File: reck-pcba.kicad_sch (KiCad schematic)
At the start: 0 parts

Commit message: Added ESP32, Power, LEDs, IMU, and GPS - Added supporting libraries - Added datasheets in the doc/datasheet folder
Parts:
- added C1, C13, C14, C17, C18, C19, C2, C20, C23, C24, C28, C29, C3, C30, C31, C4: 100nF, symbol Device:C
- added C10, C11, C15, C21, C22, C25, C6, C7: 1uF, symbol Device:C
- added C12, C9: 100n, symbol Device:C
- added C16, C5, C8: 10uF, symbol Device:C
- added C26, C27: 3.3pF, symbol Device:C
- added D1, D2, D3: LED, symbol Device:LED
- added J2: USB_C_Receptacle_USB2.0_16P, symbol reck-connectors:USB_C_Receptacle_USB2.0_16P
- added L1, L2, L3: 2.2n, symbol Device:L
- added R1, R13, R14, R15, R2, R3, R8: 5.1k, symbol Device:R
- added R10, R9: 150R, symbol Device:R
- added R11: 300R, symbol Device:R
- added R12, R6, R7: 49.9R, symbol Device:R
- added R4: 47R, symbol Device:R
- added R5: 470R, symbol Device:R
- added SW1: SW_Push, symbol Switch:SW_Push
- added TP1, TP2, TP3, TP4, TP5, TP6: TestPoint, TestPoint:TestPoint_Pad_D1.5mm, symbol Connector:TestPoint
- added U1: ESP32-C3FH4, reck-ics:QFN-32-1EP_5x5mm_P0.5mm_EP3.7x3.7mm, symbol reck-ics:ESP32-C3FH4
- added U10: USBLC6-2P6, Package_TO_SOT_SMD:SOT-666, symbol Power_Protection:USBLC6-2P6
- added U11, U7, U8, U9: WS2812B, reck-ics:WS2812B, symbol reck-ics:WS2812B
- added U12: SAM-M10Q-00B, reck-ics:SAM-M10Q, symbol reck-ics:SAM-M10Q-00B
- added U2: SN74LVC1T45DBV, Package_TO_SOT_SMD:SOT-23-6, symbol Logic_LevelTranslator:SN74LVC1T45DBV
- added U3, U4: NCP705MT33TCG, reck-ics:DFN-6-1EP_2x2mm_P0.65mm_EP1.01x1.7mm, symbol reck-ics:NCP705MT33TCG
- added U5: ISM330DHCXTR, reck-ics:LGA-14L_2.5x3.0mm_P0.5mm, symbol reck-ics:ISM330DHCXTR
- added Y2: 40MHz, symbol Device:Crystal_GND2
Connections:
- new net: U11.4 (DI), U2.4 (B)
- new net: D1.1 (K), R9.1
- new net: J2.A5 (CC1), R2.1
- new net: U11.3 (GND), U7.3 (GND), U8.3 (GND), U9.3 (GND)
- new net: U8.2 (DO), U9.4 (DI)
- new net: C26.1, L3.1, U1.1 (LNA_IN)
- new net: C27.1, L3.2
- new net: J2.A7 (D-), J2.B7 (D-), U10.1 (I/O1)
- new net: J2.A6 (D+), J2.B6 (D+), U10.3 (I/O2)
- new net: R7.2, U1.12 (MTCK)
- new net: R6.2, U1.13 (MTDO)
- new net: C13.1, L2.1, U1.2 (VDD3P3), U1.3 (VDD3P3)
- new net: R5.2, U1.28 (U0TXD)
- new net: C24.1, U1.29 (XTAL_N), Y2.3
- new net: R4.1, U1.30 (XTAL_P)
- new net: C25.1, R3.2, SW1.1, U1.7 (CHIP_EN)
- new net: C23.1, R4.2, Y2.1
- new net: D3.1 (K), R11.1
- new net: J2.B5 (CC2), R1.1
- new net: U11.2 (DO), U7.4 (DI)
- new net: D2.1 (K), R10.1
- new net: R12.2, U5.1 (SDO/SA0)
- new net: U7.2 (DO), U8.4 (DI)
- new net +3V3A: C10.1, C11.1, C28.1, C29.1, C8.1, D1.2 (A), D2.2 (A), R8.1, U12.17 (VCC), U12.2 (V_IO), U12.3 (V_BCKP), U3.1 (OUT), U5.5 (VDD_IO), U5.8 (VDD)
- new net +3V3D: C14.1, C15.1, C16.1, C17.1, C18.1, C19.1, C20.1, C21.1, C22.1, C31.1, C5.1, L2.2, R13.1, R14.1, R15.1, R3.1, U1.11 (VDD3P3_RTC), U1.17 (VDD3P3_CPU), U1.18 (VDD_SPI), U1.31 (VDDA), U1.32 (VDDA), U2.1 (VCCA), U2.5 (DIR), U4.1 (OUT)
- new net +5V: C1.1, C2.1, C3.1, C30.1, C4.1, U11.1 (VDD), U2.6 (VCCB), U7.1 (VDD), U8.1 (VDD), U9.1 (VDD)
- new net +VBUS: C9.1, D3.2 (A), J2.A4 (VBUS), J2.A9 (VBUS), J2.B4 (VBUS), J2.B9 (VBUS), L1.1, U10.5 (VBUS)
- new net +VBUS-FILT: C12.1, C6.1, C7.1, L1.2, U3.4 (EN), U3.6 (IN), U4.4 (EN), U4.6 (IN)
- new net GND: C1.2, C10.2, C11.2, C12.2, C13.2, C14.2, C15.2, C16.2, C17.2, C18.2, C19.2, C2.2, C20.2, C21.2, C22.2, C23.2, C24.2, C25.2, C26.2, C27.2, C28.2, C29.2, C3.2, C30.2, C31.2, C4.2, C5.2, C6.2, C7.2, C8.2, C9.2, J2.A1 (GND), J2.A12 (GND), J2.B1 (GND), J2.B12 (GND), R1.2, R10.2, R11.2, R2.2, R9.2, SW1.2, U1.33 (GND), U10.2 (GND), U12.1 (GND), U12.10 (GND), U12.11 (GND), U12.15 (GND), U12.16 (GND), U12.20 (GND), U12.4 (GND), U12.5 (GND), U12.6 (GND), U2.2 (GND), U3.2 (NC), U3.3 (GND), U3.5 (NC), U3.7 (EP), U4.2 (NC), U4.3 (GND), U4.5 (NC), U4.7 (EP), U5.2 (SDX), U5.3 (SCX), U5.6 (GND), U5.7 (GND), Y2.2
- new net GPIO10: U1.16 (GPIO10)
- new net GPIO8: U1.14 (GPIO8)
- new net GPIO9: U1.15 (GPIO9)
- new net GPS-EXTINT: U12.19 (EXTINT)
- new net GPS-NRESET: R8.2, U12.18 (~{RESET})
- new net GPS-TP: TP5.1, U12.7 (TIMEPULSE)
- new net IMU-CS: U5.12 (CS)
- new net IMU-INT1: U5.4 (INT1)
- new net IMU-INT2: U5.9 (INT2)
- new net LED-DOUT: U1.8 (GPIO3), U2.3 (A)
- new net MISO: R12.1, R13.2, TP6.1, U1.6 (GPIO2)
- new net MOSI: R6.1, TP4.1, U5.14 (SDA)
- new net SCL: R15.2, U1.9 (MTMS)
- new net SCLK: R7.1, TP3.1, U5.13 (SCL)
- new net SDA: R14.2, U1.10 (MTDI)
- new net UART0-RX: TP1.1, U1.27 (U0RXD), U12.13 (TXD)
- new net UART0-TX: R5.1, TP2.1, U12.14 (RXD)
- new net USB-DN: U1.25 (GPIO18), U10.6 (I/O1)
- new net USB-DP: U1.26 (GPIO19), U10.4 (I/O2)
- no-connect marks 0 -> 15
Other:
- note added: "GPIO2 MUST BE FLOATING GPIO8 MUST BE FLOATING GPIO9 MUST BE PULL-UP (PULL-UP INTERNAL) GPIO10 SPI2 CS0"
- note added: "Near VDD3P3_CPU"
- note added: "Near VDD3P3_RTC"
- note added: "Near VDD_A"
- note added: "Near VDD_SPI"
- note added: "Z=35R+10j"
- note added: "Z=50R"

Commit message: Added new uC, Power, and Motor support - Updated ESP32-C3 to ESP32-S3 due to GPIO constraints - Using two buck regulators for servo 5V power and board 3V3
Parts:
- removed C5: 10uF, symbol Device:C
- removed R6: 49.9R, symbol Device:R
- removed SW1: SW_Push, symbol Switch:SW_Push
- removed TP1, TP2, TP3, TP4, TP5, TP6: TestPoint, TestPoint:TestPoint_Pad_D1.5mm, symbol Connector:TestPoint
- removed U1: ESP32-C3FH4, reck-ics:QFN-32-1EP_5x5mm_P0.5mm_EP3.7x3.7mm, symbol reck-ics:ESP32-C3FH4
- removed U10: USBLC6-2P6, Package_TO_SOT_SMD:SOT-666, symbol Power_Protection:USBLC6-2P6
- removed U3, U4: NCP705MT33TCG, reck-ics:DFN-6-1EP_2x2mm_P0.65mm_EP1.01x1.7mm, symbol reck-ics:NCP705MT33TCG
- removed Y2: 40MHz, symbol Device:Crystal_GND2
- added C32, C33: 100nF, symbol Device:C
- added C34: 4.7nF, symbol Device:C
- added C36: 1uF, symbol Device:C
- added C41: 10uF, symbol Device:C
- added C5: 47uF, symbol Device:C_Polarized
- added D4: LED, symbol Device:LED
- added J4: Conn_01x03_Pin, Connector_PinHeader_2.54mm:PinHeader_1x03_P2.54mm_Vertical, symbol Connector:Conn_01x03_Pin
- added R16: 49.9R, symbol Device:R
- added R17, R24, R31, R32, R33: 5.1k, symbol Device:R
- added R23: R_Photo, symbol Device:R_Photo
- added SW1, SW2, SW3, SW4: PTS810_SJM_250_SMTR_LFS, reck-switches:PTS810_SJM_250_SMTR_LFS, symbol reck-switches:PTS810_SJM_250_SMTR_LFS
- added TH1: Thermistor_NTC, symbol Device:Thermistor_NTC
- added U1: ECS-2520S33-400-FN-TR, Oscillator:Oscillator_SMD_EuroQuartz_XO32-4Pin_3.2x2.5mm, symbol Oscillator:KC2520Z
- added U10: SN74LVC1T45DBV, Package_TO_SOT_SMD:SOT-23-6, symbol Logic_LevelTranslator:SN74LVC1T45DBV
- added U13: MCP4728, Package_SO:MSOP-10_3x3mm_P0.5mm, symbol Analog_DAC:MCP4728
- added U3: DRV8231ADSGR, Package_SON:WSON-8-1EP_2x2mm_P0.5mm_EP0.9x1.6mm, symbol reck-ics:DRV8231ADSGR
- added U4: USBLC6-2P6, Package_TO_SOT_SMD:SOT-666, symbol Power_Protection:USBLC6-2P6
- added U6: ESP32-S3FN8, reck-ics:QFN-56-1EP_7x7mm_P0.4mm_EP4x4mm, symbol reck-ics:ESP32-S3FN8
- C12, C9: value 100n -> 100nF
- C23: value 100nF -> 20pF
- C6: value 1uF -> 100nF
- C7: value 1uF -> 100n
- C8: value 10uF -> 100n
- J2: footprint (none) -> Connector_USB:USB_C_Receptacle_GCT_USB4105-xx-A_16P_TopMnt_Horizontal
- R1: value 5.1k -> 1M
- R10, R9: value 150R -> 330R
- R11: value 300R -> 660R
- R14: value 5.1k -> 499R
- R15: value 5.1k -> 330R
- R4: value 47R -> 5.1k
- R5: value 470R -> 5.1k
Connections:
- net +5V is gone; now on net +VBUS-FILT: C1.1, C2.1, C3.1, C30.1, C4.1, U11.1 (VDD), U2.6 (VCCB), U7.1 (VDD), U8.1 (VDD), U9.1 (VDD)
- net +VBUS: now also C7.1, U4.5 (VBUS); no longer C9.1, D3.2 (A)
- net +VBUS-FILT: now also C8.1, D3.2 (A); no longer C12.1, C6.1, C7.1
- net GND: now also R15.2, U11.3 (GND), U7.3 (GND), U8.3 (GND), U9.3 (GND), C32.2, C33.2, C36.2, C41.2, C5.2, J4.3 (Pin_3), R17.2, R24.2, R33.2, SW1.1, SW1.2, SW2.1, SW2.2, SW3.1, SW3.2, SW4.1, SW4.2, U1.2 (GND), U10.2 (GND), U13.10 (VSS), U13.4 (~{LDAC}), U3.7 (GND), U3.9 (EP), U6.57 (GND); no longer C23.2, R1.2
- net IMU-CS: now also R32.2
- net MISO: now also R4.2, U6.18 (GPIO13/MISO); no longer R13.2
- net MOSI: now also R16.1
- net SCL: now also U13.2 (SCL); no longer R15.2
- net SDA: now also U13.3 (SDA); no longer R14.2
- net UART0-RX: now also U6.50 (U0RXD/GPIO44)
- net UART0-TX: now also R14.2; no longer R5.1
- net USB-DN: now also U4.6 (I/O1), U6.25 (USB_D-/GPIO19)
- net USB-DP: now also U4.4 (I/O2), U6.26 (USB_D+/GPIO20)
- net at J2.A5 (CC1): now also R17.1; no longer R2.1
- net at C26.1, L3.1: now also U6.1 (LNA_IN)
- net at J2.A7 (D-), J2.B7 (D-): now also U4.1 (I/O1)
- net at J2.A6 (D+), J2.B6 (D+): now also U4.3 (I/O2)
- net at R7.2: now also U6.17 (GPIO12/SCLK)
- net at C13.1, L2.1: now also U6.2 (VDD3P3), U6.3 (VDD3P3)
- net BOOT-SEL: now reaches R5.2
- net BOOT-SEL: now also SW1.3, SW1.4
- net +3V3: now reaches C24.1
- net +3V3: now also C10.1, C11.1, C14.1, C15.1, C16.1, C17.1, C18.1, C19.1, C20.1, C22.1, C28.1, C29.1, C31.1, C9.1, D2.2 (A), L2.2, R13.1, R3.1, R4.1, R5.1, R8.1, U12.17 (VCC), U12.2 (V_IO), U12.3 (V_BCKP), U2.1 (VCCA), U2.5 (DIR), U5.5 (VDD_IO), U5.8 (VDD), C33.1, C36.1, C41.1, R23.1, R31.1, R32.1, U1.4 (VCC), U10.1 (VCCA), U10.5 (DIR), U13.1 (VDD), U3.4 (VREF), U6.20 (VDD3P3_RTC), U6.46 (VDD3P3_CPU), U6.55 (VDDA), U6.56 (VDDA)
- net ESP-NRESET: now reaches C25.1, R3.2
- net ESP-NRESET: now also SW2.3, SW2.4, U6.4 (CHIP_PU)
- net at C23.1: now also U6.54 (XTAL_P); no longer R4.2
- net at J2.B5 (CC2): now also R2.1; no longer R1.1
- net at J2.S1 (SHIELD): now also R1.1, C34.1
- removed net +3V3A: C10.1, C11.1, C28.1, C29.1, C8.1, D1.2 (A), D2.2 (A), R8.1, U12.17 (VCC), U12.2 (V_IO), U12.3 (V_BCKP), U5.5 (VDD_IO), U5.8 (VDD)
- removed net +3V3D: C14.1, C15.1, C16.1, C17.1, C18.1, C19.1, C20.1, C21.1, C22.1, C31.1, L2.2, R13.1, R14.1, R15.1, R3.1, U2.1 (VCCA), U2.5 (DIR)
- net GPS-TP renamed GPS-TIMEPULSE
- net LED-DOUT renamed DOUT-LED
- new net: D4.1 (K), R15.1
- new net: R16.2, U6.16 (GPIO11/MOSI)
- new net: C23.2, U1.3 (CLK)
- new net: R33.1, U3.1 (IPROPI)
- new net: J4.2 (Pin_2), U10.4 (B)
- new net: R14.1, U6.49 (U0TXD/GPIO43)
- new net +12V-EXT: C5.1, C6.1, U3.5 (VM)
- new net +5V-EXT: C12.1, J4.1 (Pin_1), U10.6 (VCCB)
- new net +VDD_SPI: C21.1, C32.1, U6.29 (VDD_SPI)
- new net AOUT-A: U13.6 (VOUTA)
- new net AOUT-B: U13.7 (VOUTB)
- new net AOUT-C: U13.8 (VOUTC)
- new net AOUT-D: U13.9 (VOUTD)
- new net BUTTON0: R31.2, SW4.3, SW4.4
- new net BUTTON1: R13.2, SW3.3, SW3.4
- new net LED0: D4.2 (A)
- new net LED1: D1.2 (A)
- new net MOTOR-IN1: U3.3 (IN1)
- new net MOTOR-IN2: U3.2 (IN2)
- new net MOTOR-OUT1: U3.6 (OUT1)
- new net MOTOR-OUT2: U3.8 (OUT2)
- new net PWM-SERVO: U10.3 (A)
- new net SHIELD: C34.2, R1.2, U4.2 (GND)
- new net V-PHOTO-RES: R23.2, R24.1
- no-connect marks 15 -> 13
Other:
- added sheet power (power.kicad_sch)
- note added: "0.43A Motor Current"
- note added: "BOOT SEL"
- note added: "BUTTON INPUTS"
- note added: "DIGITAL TO ANALOG CONVERTER (DAC)"
- note added: "GPS MODULE"
- note added: "HW RESET"
- note added: "I2C Address: 0x60"
- note added: "INDICATION LEDS"
- note added: "INERTIAL MEASUREMENT UNIT"
- note added: "LED STRIP"
- note added: "RECK (Resourceful Embedded Circuity Kit) PCBA"
- note added: "SERVO"
- note added: "USBC POWER AND DATA INPUT"
- note added: "USER BUTTON0"
- note added: "USER BUTTON1"
- note removed: "GPIO2 MUST BE FLOATING GPIO8 MUST BE FLOATING GPIO9 MUST BE PULL-UP (PULL-UP INTERNAL) GPIO10 SPI2 CS0"
- note removed: "Near VDD_SPI"
- moved on the sheet: C1, C10, C11, C13, C14, C15, C16, C17, C18, C19, C2, C20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

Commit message: Full Schematics Complete - Changed uC to ESP32-S3-WROOM-2 to allow for pinout discussion. - Moved buck regulators to main sheet. - Added titles and descriptions to each Sensor, Interface, or concept. - Added LCD. - Changed DAC to single-channel variant. - Added I2C Laser Time-of-Flight Sensor. - Added Environmental Sensor. - Updated pinout on uC.
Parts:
- removed C21: 1uF, symbol Device:C
- removed C23: 20pF, symbol Device:C
- removed C26: 3.3pF, symbol Device:C
- removed C31, C33: 100nF, symbol Device:C
- removed C41: 10uF, symbol Device:C
- removed L3: 2.2n, symbol Device:L
- removed R12, R16, R7: 49.9R, symbol Device:R
- removed R33, R4, R8: 5.1k, symbol Device:R
- removed SW3: PTS810_SJM_250_SMTR_LFS, reck-switches:PTS810_SJM_250_SMTR_LFS, symbol reck-switches:PTS810_SJM_250_SMTR_LFS
- removed TH1: Thermistor_NTC, symbol Device:Thermistor_NTC
- removed U1: ECS-2520S33-400-FN-TR, Oscillator:Oscillator_SMD_EuroQuartz_XO32-4Pin_3.2x2.5mm, symbol Oscillator:KC2520Z
- removed U10, U2: SN74LVC1T45DBV, Package_TO_SOT_SMD:SOT-23-6, symbol Logic_LevelTranslator:SN74LVC1T45DBV
- removed U12: SAM-M10Q-00B, reck-ics:SAM-M10Q, symbol reck-ics:SAM-M10Q-00B
- removed U13: MCP4728, Package_SO:MSOP-10_3x3mm_P0.5mm, symbol Analog_DAC:MCP4728
- removed U6: ESP32-S3FN8, reck-ics:QFN-56-1EP_7x7mm_P0.4mm_EP4x4mm, symbol reck-ics:ESP32-S3FN8
- added BZ1: CEM-1206S, reck-audio:CEM-1206S, symbol reck-audio:CEM-1206S
- added C2, C3, C37, C4, C5: 10uF, symbol Device:C
- added C34, C35: 100nF, symbol Device:C
- added D2: LED, symbol Device:LED
- added D3, D8: D_Schottky, symbol Device:D_Schottky
- added D5: D_Zener, symbol Device:D_Zener
- added J2, J3: 575-4, reck-connectors:575-4, symbol reck-connectors:575-4
- added J5: Conn_01x03_Pin, Connector_PinHeader_2.54mm:PinHeader_1x03_P2.54mm_Vertical, symbol Connector:Conn_01x03_Pin
- added J6: TBL002A-350-02GR-2OR, reck-connectors:TBL002A-350-02GR-2OR, symbol reck-connectors:TBL002A-350-02GR-2OR
- added Q1: BC846, Package_TO_SOT_SMD:SOT-23, symbol Transistor_BJT:BC846
- added R17, R18, R19, R22, R24, R25, R26, R28, R30, R31: 5.1k, symbol Device:R
- added R20: 330R, symbol Device:R
- added R21: 16k, symbol Device:R
- added R23: 26.7k, symbol Device:R
- added R27, R6: 1k, symbol Device:R
- added R3: 3.3k, symbol Device:R
- added RV1, RV2: 10k, symbol Device:R_Potentiometer
- added TP1, TP10, TP11, TP12, TP13, TP2, TP3, TP4, TP5, TP6, TP7, TP8, TP9: TestPoint, symbol Connector:TestPoint
- added U13: VL53L0CXV0DH1, Sensor_Distance:ST_VL53L1x, symbol Sensor_Distance:VL53L0CXV0DH1
- added U14: MCP4725A0T-E/CH, Package_TO_SOT_SMD:SOT-23-6, symbol Analog_DAC:MCP4725xxx-xCH
- added U16: BME280, Package_LGA:Bosch_LGA-8_2.5x2.5mm_P0.65mm_ClockwisePinNumbering, symbol Sensor:BME280
- added U2: LCD2X16, reck-ics:LCD2X16, symbol reck-ics:LCD2X16
- added U3, U4: TPS62912RPUR, reck-ics:VQFN-HR-10_2x2mm, symbol reck-ics:TPS62912RPUR
- added U5, U9: TXU0104PWR, Package_SO:TSSOP-14_4.4x5mm_P0.65mm, symbol reck-ics:TXU0104PWR
- added U8: ESP32-S3-WROOM-2, RF_Module:ESP32-S3-WROOM-2, symbol RF_Module:ESP32-S3-WROOM-2
- C11, C15, C22, C36: value 1uF -> 100nF
- C13, C14, C17, C18, C19, C24: value 100nF -> 22uF
- C16: value 10uF -> 22uF
- C27: value 3.3pF -> 100nF
- C7, C8: value 100n -> 2.2nF
- C9: value 100nF -> 1uF
- J1: renamed from J2; value USB_C_Receptacle_USB2.0_16P -> USB4105-GF-A
- L1, L2: value 2.2n -> 2.2uH
- R13: value 5.1k -> 6.04k
- R14: value 499R -> 6.04k
- R15: renamed from R23; value R_Photo -> 02-LDR4
- R8: renamed from R11; value 660R -> 1k
- renumbered C34 to C1, C1 to C21, C2 to C23, C3 to C25, C5 to C26, C6 to C28, C4 to C29, C29 to C31, C28 to C33, C25 to C6, D3 to D4, D2 to D6, D4 to D7, R3 to R11, R15 to R12, R24 to R16, R31 to R2, R32 to R29, R2 to R4, R17 to R5, R5 to R7, SW4 to SW1, SW1 to SW2, SW2 to SW3, U4 to U1, U8 to U10, U3 to U11, U9 to U12, U5 to U15, U11 to U6
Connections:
- net +VDD_SPI is gone; now on net +3V3: C32.1
- net BUTTON1 is gone; now on net GND: R13.2
- net LED1 is gone; now on net +12V-EXT: D1.2 (A)
- net UART0-TX is gone; now on net GND: R14.2
- net +12V-EXT: now also C8.1, C3.1, C5.1, D3.1 (K), D5.1 (K), U4.1 (EN/SYNC), U4.6 (VIN)
- net +3V3: now also C13.1, C21.1, C23.1, C25.1, C27.1, C29.1, L1.2, U10.1 (VDD), U12.1 (VDD), U6.1 (VDD), U7.1 (VDD), BZ1.1, C34.1, C35.1, C37.1, D8.1 (K), R21.1, R25.1, R26.1, R28.1, R30.1, R31.1, RV2.1, U13.1 (AVDDVCSEL), U13.11 (AVDD), U14.3 (VDD), U16.6 (VDDIO), U16.8 (VDD), U3.3 (VO), U5.1 (VCCA), U5.8 (OE), U8.2 (3V3), U9.1 (VCCA), U9.8 (OE); no longer C10.1, C11.1, C14.1, C15.1, C17.1, C19.1, C22.1, C9.1, L2.2, R13.1
- net +5V-EXT: now also C14.1, C17.1, C19.1, L2.2, D2.2 (A), R23.1, U4.3 (VO); no longer C12.1
- net +VBUS: now also C22.1, C30.1, D4.2 (A), R10.1, C2.1, C4.1, RV1.1, U2.2 (VDD), U3.1 (EN/SYNC), U3.6 (VIN), U5.14 (VCCB), U9.14 (VCCB); no longer L1.1
- net BOOT-SEL: now also U8.27 (IO0)
- net GND: now also C2.2, C3.2, C34.2, C35.2, C37.2, C4.2, C5.2, D5.2 (A), J3.1, J5.3 (Pin_3), Q1.2 (E), R22.2, R24.2, R27.2, R3.2, R6.2, RV1.3, RV2.3, TP12.1, U13.12 (GND), U13.2 (AVSSVCSEL), U13.3 (GND), U13.4 (GND), U13.6 (GND), U14.2 (VSS), U14.6 (A0), U16.1 (GND), U16.7 (GND), U2.1 (VSS), U2.16 (LEDK), U2.5 (R/W), U3.4 (PGND), U3.7 (PSNS), U4.4 (PGND), U4.7 (PSNS), U5.7 (GND), U8.1 (GND), U8.40 (GND), U8.41 (GND), U9.7 (GND); no longer R10.2
- net IMU-CS: now also TP9.1, U8.8 (IO15)
- net IMU-INT1: now also U8.9 (IO16)
- net MOTOR-IN1: now also TP1.1, U8.4 (IO4)
- net MOTOR-IN2: now also TP2.1, U8.5 (IO5)
- net MOTOR-OUT1: now also J6.1
- net MOTOR-OUT2: now also J6.2
- net PWM-SERVO: now also U5.3 (A2), U8.6 (IO6)
- net USB-DN: now also U8.13 (USB_D-/IO19)
- net USB-DP: now also U8.14 (USB_D+/IO20)
- net PWM-LED: now reaches U6.4 (DI)
- net PWM-LED: now also U8.7 (IO7)
- net at U11.1 (IPROPI): now also R27.1
- net PWM-SERVO-5V: now reaches J4.2 (Pin_2)
- net PWM-SERVO-5V: now also U5.12 (B2Y)
- net at L2.1: now also U4.2 (SW); no longer C13.1
- net at R14.1: now also U4.10 (S-CONF)
- net at R9.1: now also D6.1 (K); no longer D1.1 (K)
- net SPI-MISO: now reaches U15.1 (SDO/SA0)
- net SPI-MISO: now also R28.2, TP8.1, U16.5 (SDO), U8.21 (IO13)
- removed net +VBUS-FILT: C21.1, C23.1, C25.1, C29.1, C30.1, C8.1, D4.2 (A), L1.2, U10.1 (VDD), U12.1 (VDD), U6.1 (VDD), U7.1 (VDD)
- net BUTTON0 renamed USER-BUTTON
- net USER-BUTTON: now also U8.11 (IO18)
- net ESP-NRESET renamed ESP-EN
- net ESP-EN: now also U8.3 (EN)
- net IMU-INT2: no longer names the net of U15.9 (INT2)
- net LED0 renamed USER-LED
- net USER-LED: now also U8.10 (IO17)
- net MOSI renamed SPI-MOSI
- net SPI-MOSI: now also TP6.1, U16.3 (SDI), U8.19 (IO11)
- net SCLK renamed SPI-SCLK
- net SPI-SCLK: now also TP7.1, U16.4 (SCK), U8.20 (IO12)
- net V-PHOTO-RES renamed V-PHOTO
- net V-PHOTO: now also R17.2
- new net: BZ1.2, D8.2 (A), Q1.3 (C)
- new net: R21.2, R22.1, U3.9 (FB)
- new net: D3.2 (A), J2.1
- new net: R13.1, U3.10 (S-CONF)
- new net: L1.1, U3.2 (SW)
- new net: R23.2, R24.1, U4.9 (FB)
- new net: Q1.1 (B), R20.2
- new net: D1.1 (K), R3.1
- new net: C10.1, U4.8 (NR/SS)
- new net: C9.1, U3.8 (NR/SS)
- new net: R10.2, U2.15 (LEDA)
- new net: R31.2, U13.5 (XSHUT)
- new net: D2.1 (K), R6.1
- new net ATMO-CS: R30.2, U16.2 (CSB), U8.22 (IO14)
- new net I2C-SCL: R26.2, TP5.1, U13.10 (SCL), U14.5 (SCL), U8.18 (IO10)
- new net I2C-SDA: R25.2, TP4.1, U13.9 (SDA), U14.4 (SDA), U8.17 (IO9)
- new net LCD-DB4: U8.32 (MTCK/IO39), U9.2 (A1)
- new net LCD-DB4-5V: U2.11 (DB4), U9.13 (B1Y)
- new net LCD-DB5: U8.33 (MTDO/IO40), U9.3 (A2)
- new net LCD-DB5-5V: U2.12 (DB5), U9.12 (B2Y)
- new net LCD-DB6: U8.34 (MTDI/IO41), U9.4 (A3)
- new net LCD-DB6-5V: U2.13 (DB6), U9.11 (B3Y)
- new net LCD-DB7: U8.35 (MTMS/IO42), U9.5 (A4)
- new net LCD-DB7-5V: U2.14 (DB7), U9.10 (B4Y)
- new net LCD-EN: U5.4 (A3), U8.23 (IO21)
- new net LCD-EN-5V: U2.6 (E), U5.11 (B3Y)
- new net LCD-RS: U5.5 (A4), U8.31 (IO38)
- new net LCD-RS-5V: U2.4 (RS), U5.10 (B4Y)
- new net LCD-VO: RV1.2, U2.3 (VO)
- new net PWM-BUZZER: R20.1, TP3.1, U8.12 (IO8)
- new net UART1-RX: J5.2 (Pin_2), TP11.1, U8.16 (IO46)
- new net UART1-TX: J5.1 (Pin_1), TP10.1, U8.26 (IO45)
- new net V-DAC: R19.2, TP13.1, U14.1 (VOUT)
- new net V-DAC-FILT: C11.1, R19.1, U8.15 (IO3)
- new net V-PHOTO-FILT: C15.1, R17.1, U8.39 (IO1)
- new net V-POT: R18.2, RV2.2
- new net V-POT-FILT: C12.1, R18.1, U8.38 (IO2)
- no-connect marks 13 -> 19
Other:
- removed sheet power
- note added: "12V BANANA CONNECTORS"
- note added: "2.2A Motor Current"
- note added: "2x16 LIQUID CRYSTAL DISPLAY (LCD)"
- note added: "3-Pin Header"
- note added: "3V3 to 5V Logic Level Conversion"
- note added: "4Bit Parallel Interface"
- note added: "ADVANCED TRAINING"
- note added: "ANTIALIASING FILTER"
- note added: "ATMOSPHERIC SENSOR"
- note added: "Analog Input"
- note added: "Analog Output"
- note added: "BASIC TRAINING"
- note added: "Buck Regulators"
- note added: "CONNECTORS AND POWER"
- note added: "Custom Printed Circuit Board Assembly (PCBA) talored to teach all of the basic and advanced embedded use cases seen at the HIVE Makerspace. Integrates a ESP32 microcontroller, probe-able SPI, I2C, UART, motor drivers, servo drivers, power electronics, and commonly used sensors."
- note added: "DIGITAL-TO-ANALOG CONVERTER (DAC)"
- note added: "Digital Inputs"
- note added: "Digital Output"
- note added: "ESP32-S3 MICROCONTROLLER"
- note added: "I2C Device - Address: 0x52"
- note added: "I2C Device - Address: 0x60"
- note added: "I2C Pullups"
- note added: "INERTIAL MEASUREMENT UNIT (IMU)"
- note added: "IR LASER TOF SENSOR"
- note added: "Low-pass Filtered Analog Inputs"
- note added: "MAGNETIC BUZZER"
- note added: "MICROCONTROLLER"
- note added: "MISO Pullup"
- note added: "MOTOR CONNECTOR"
- note added: "MOTOR DRIVER"
- note added: "Motor and Servo Supply"
- note added: "PHOTORESISTOR"
- note added: "POTENTIOMETER"
- note added: "PWM Interface"
- note added: "PWM Interface - 3-Pin Header"
- note added: "PWM Sound Output"
- note added: "Power and Data IO"
- note added: "Probable Interfaces"
- note added: "RECK PCBA (Resourceful Embedded Circuity Kit Printed Circuit Board Assembly)"
- note added: "SERVO CONNECTOR"
- note added: "SPI Device - CS: IO14"
- note added: "SPI Device - CS: IO15"
- note added: "Spring-lock Terminal"
- note added: "Step-down Power Conversion"
- note added: "System on a chip (SOC) microcontroller with integrated Wi-Fi and dual-mode Bluetooth"
- note added: "TEST POINTS"
- note added: "UART CONNECTOR"
- note added: "USB-C CONNECTOR"
- note added: "USER BUTTON"
- note added: "VOLTAGE TRANSLATORS"
- note removed: "0.43A Motor Current"
- note removed: "DIGITAL TO ANALOG CONVERTER (DAC)"
- note removed: "GPS MODULE"
- note removed: "I2C Address: 0x60"
- note removed: "INERTIAL MEASUREMENT UNIT"
- note removed: "Near VDD3P3_CPU"
- note removed: "Near VDD3P3_RTC"
- note removed: "Near VDD_A"
- note removed: "RECK (Resourceful Embedded Circuity Kit) PCBA"
- note removed: "SERVO"
- note removed: "USBC POWER AND DATA INPUT"
- note removed: "USER BUTTON0"
- note removed: "USER BUTTON1"
- note removed: "Z=35R+10j"
- note removed: "Z=50R"
- title: RECK PCBA Top Sheet -> RECK PCBA
- moved on the sheet: C1, C21, C23, C25, C26, C28, C29, C31, C33, C6, D4, D6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

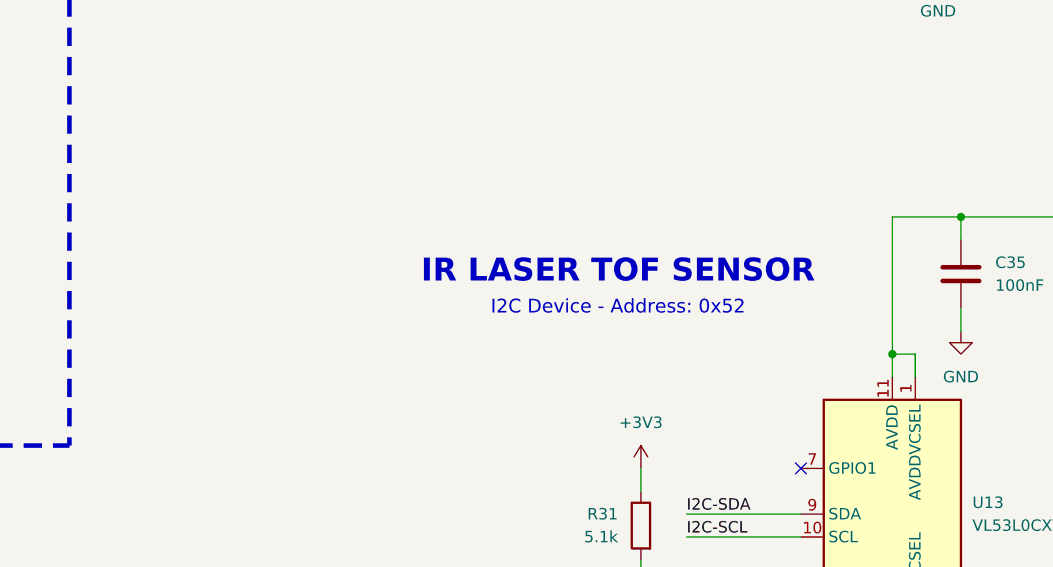
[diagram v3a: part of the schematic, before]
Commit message: Updated IR TOF Sensor Wording - Changed "IR LASER TOF SENSOR" to "IR TIME-OF-FLIGHT (TOF) SENSOR". - Updated Schematic. - Updated PDF.
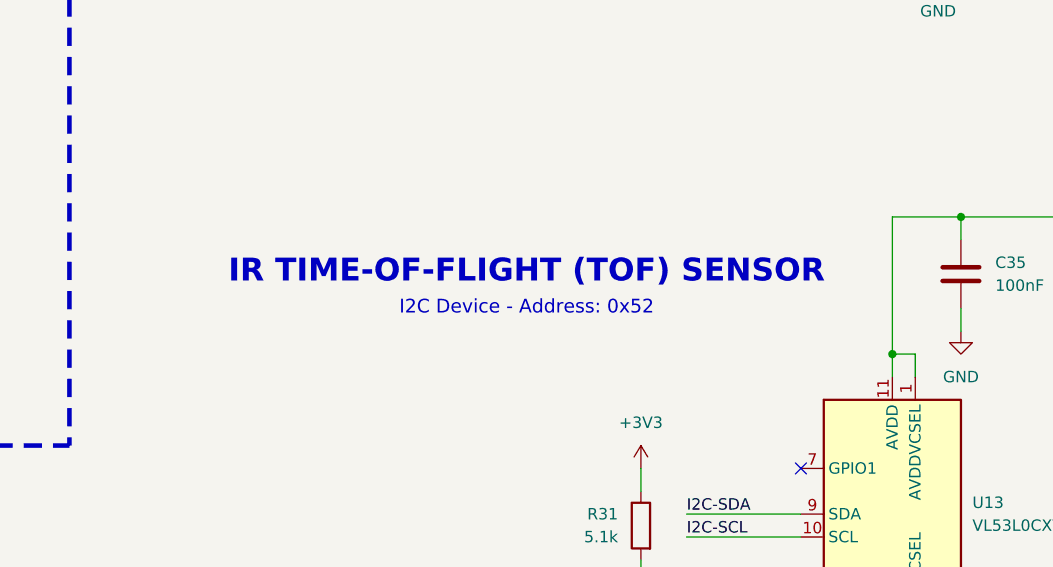
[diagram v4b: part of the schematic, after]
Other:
- note added: "IR TIME-OF-FLIGHT (TOF) SENSOR"
- note removed: "IR LASER TOF SENSOR"
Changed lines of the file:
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@@
 		)
 	)
-	(text "IR LASER TOF SENSOR"
-		(exclude_from_sim no)
-		(at 505.46 238.76 0)
+	(text "IR TIME-OF-FLIGHT (TOF) SENSOR"
+		(exclude_from_sim no)
+		(at 495.3 238.76 0)
 		(effects
 			(font
@@
 	(text "I2C Device - Address: 0x52"
 		(exclude_from_sim no)
-		(at 505.46 241.3 0)
-		(effects
-			(font
+		(at 495.3 241.3 0)
+		(effects
+			(font
